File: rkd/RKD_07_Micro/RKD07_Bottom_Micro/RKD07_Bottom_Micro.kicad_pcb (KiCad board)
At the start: 2 copper layers, 98.8 x 85.7 mm, 15 parts

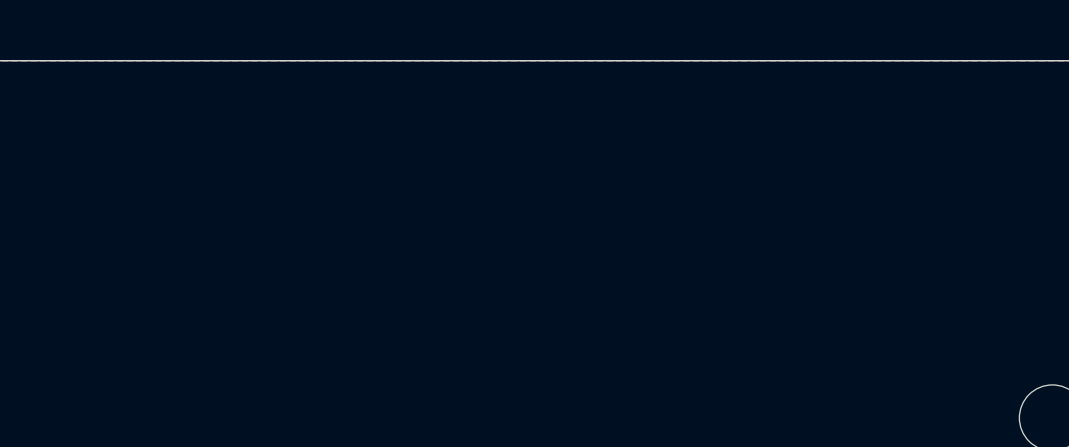
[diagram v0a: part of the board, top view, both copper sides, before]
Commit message: miniシリーズのネジ穴追加
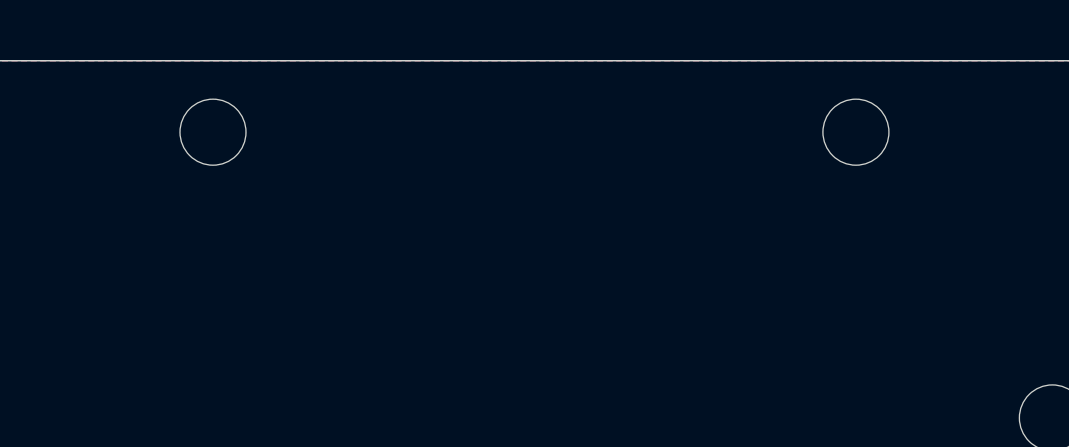
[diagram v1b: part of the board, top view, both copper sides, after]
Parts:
- added Ref**: Val**, kbd_Hole:m2_Screw_Hole, F.Cu at (57.1, 21.4)
- added Ref**: Val**, kbd_Hole:m2_Screw_Hole, F.Cu at (78.6, 21.4)
